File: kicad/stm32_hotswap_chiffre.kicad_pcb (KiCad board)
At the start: 2 copper layers, 227.3 x 85 mm, 108 parts, among them J1 USB_C_Receptacle_USB2.0, J101 Conn_01x03_Female, J2 OLED I2C, SW1 SW_Push, SW10 SW_Push, SW11 SW_Push, SW12 SW_Push, SW13 SW_Push, SW14 SW_Push, SW15 SW_Push, SW16 SW_Push, SW17 SW_Push, SW18 SW_Push, SW19 SW_Push, SW2 SW_Push, SW20 SW_Push, SW21 SW_Push, SW22 SW_Push, SW23 SW_Push, SW24 SW_Push, SW25 SW_Push, SW26 SW_Push, SW27 SW_Push, SW28 SW_Push, SW29 SW_Push, SW3 SW_Push, SW30 SW_Push, SW31 SW_Push, SW32 SW_Push, SW33 SW_Push, SW34 SW_Push, SW35 SW_Push, SW36 Rotary_Encoder_Switch, SW37 SKQGABE010, SW4 SW_Push, SW5 SW_Push, SW6 SW_Push, SW7 SW_Push, SW8 SW_Push, SW9 SW_Push, U1 STM32F072CBT6, U2 PRTR5V0U2X, U3 XC6206PxxxMR-Regulator_Linear

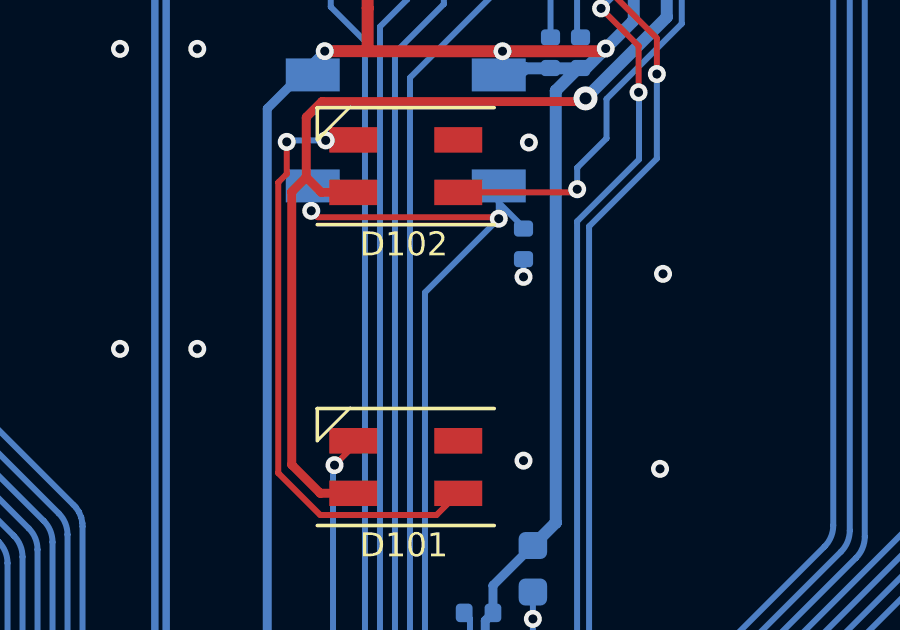
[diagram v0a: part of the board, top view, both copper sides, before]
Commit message: adding front LED bypass jumper
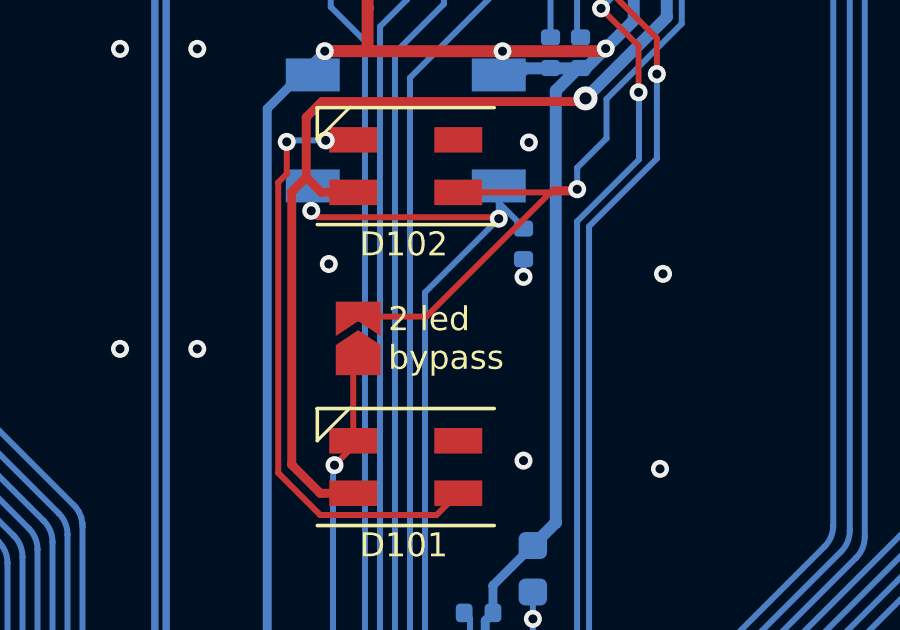
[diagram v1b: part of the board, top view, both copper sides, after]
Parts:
- added led: Jumper_2_Open, Jumper:SolderJumper-2_P1.3mm_Open_TrianglePad1.0x1.5mm, F.Cu at (145.1, 108.5)
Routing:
- net Net-(D102-DOUT): track 60.6 -> 69.7 mm
- net RGB: track 7.39 -> 10.1 mm
- net GND: vias 128 -> 129
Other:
- board text added: "2 led bypass"
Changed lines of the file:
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@@
   (title_block
     (title "Le Chiffre STM32")
-    (date "2023-07-09")
-    (rev "v0.2")
+    (date "2023-07-13")
+    (rev "v0.2.1")
     (company "sporkus")
   )
@@
     )
   )
+  (footprint "Jumper:SolderJumper-2_P1.3mm_Open_TrianglePad1.0x1.5mm" (layer "F.Cu")
+    (at 145.054472 108.55 90)
+    (descr "SMD Solder Jumper, 1x1.5mm Triangular Pads, 0.3mm gap, open")
+    (tags "solder jumper open")
+    (property "Sheetfile" "rgb.kicad_sch")
+    (property "Sheetname" "RGB leds")
+    (property "ki_description" "Jumper, 2-pole, open")
+    (property "ki_keywords" "Jumper SPST")
+    (attr exclude_from_pos_files)
+    (fp_text reference "led" (at 0.8 4.74 180) (layer "F.SilkS") hide
+        (effects (font (size 0.8 0.8) (thickness 0.15)))
+    )
+    (fp_text value "Jumper_2_Open" (at 0 1.9 90) (layer "F.Fab")
+        (effects (font (size 1 1) (thickness 0.15)))
+    )
+    (fp_line (start -1.65 -1.25) (end -1.65 1.25)
+      (stroke (width 0.05) (type solid)) (layer "F.CrtYd"))
+    (fp_line (start -1.65 -1.25) (end 1.65 -1.25)
+      (stroke (width 0.05) (type solid)) (layer "F.CrtYd"))
+    (fp_line (start 1.65 1.25) (end -1.65 1.25)
+      (stroke (width 0.05) (type solid)) (layer "F.CrtYd"))
+    (fp_line (start 1.65 1.25) (end 1.65 -1.25)
+      (stroke (width 0.05) (type solid)) (layer "F.CrtYd"))
+    (pad "1" smd custom (at -0.725 0 90) (size 0.3 0.3) (layers "F.Cu" "F.Mask")
+      (net 8 "RGB") (pinfunction "A") (pintype "passive") (zone_connect 2) (thermal_bridge_angle 45)
+      (options (clearance outline) (anchor rect))
+      (primitives
+        (gr_poly
+          (pts
+            (xy 1 0)
+            (xy 0.5 0.75)
+            (xy -0.5 0.75)
+            (xy -0.5 -0.75)
+            (xy 0.5 -0.75)
+          )
+          (width 0) (fill yes))
+      ))
+    (pad "2" smd custom (at 0.725 0 90) (size 0.3 0.3) (layers "F.Cu" "F.Mask")
+      (net 78 "Net-(D102-DOUT)") (pinfunction "B") (pintype "passive") (zone_connect 2) (thermal_bridge_angle 45)
+      (options (clearance outline) (anchor rect))
+      (primitives
+        (gr_poly
+          (pts
+            (xy 0.5 0.75)
+            (xy -0.65 0.75)
+            (xy -0.15 0)
+            (xy -0.65 -0.75)
+            (xy 0.5 -0.75)
+          )
+          (width 0) (fill yes))
+      ))
+  )
   (footprint "modified_footrprints:RotaryEncoder_EC11_no_mp" (layer "F.Cu")
     (at 146.639472 84.358057 90)
@@
     (effects (font (size 0.8 0.8) (thickness 0.15) bold) (justify mirror))
   )
+  (gr_text "2 led\nbypass" (at 146.054472 108.55) (layer "F.SilkS")
+    (effects (font (size 0.8 0.8) (thickness 0.15)) (justify left))
+  )
   (gr_text "sda" (at 150.550698 94.075) (layer "F.SilkS")
     (effects (font (size 0.8 0.8) (thickness 0.15) bold))
@@
   (via (at 256.139472 100.475) (size 0.6) (drill 0.3) (layers "F.Cu" "B.Cu") (free) (net 1))
   (via (at 146.529979 124.313523) (size 0.6) (drill 0.3) (layers "F.Cu" "B.Cu") (free) (net 1))
+  (via (at 144.074472 106.07) (size 0.6) (drill 0.3) (layers "F.Cu" "B.Cu") (free) (net 1))
   (via (at 143.589472 121.058057) (size 0.6) (drill 0.3) (layers "F.Cu" "B.Cu") (net 1))
   (via (at 149.628287 124.077799) (size 0.6) (drill 0.3) (layers "F.Cu" "B.Cu") (net 1))
@@
   (segment (start 145.689473 88.858056) (end 147.797528 86.75) (width 0.2) (layer "B.Cu") (net 7))
   (segment (start 144.814327 112.225145) (end 144.814327 112.038203) (width 0.2) (layer "F.Cu") (net 8))
+  (segment (start 144.889472 111.963058) (end 144.889472 109.44) (width 0.2) (layer "F.Cu") (net 8))
+  (segment (start 144.889472 109.44) (end 145.054472 109.275) (width 0.2) (layer "F.Cu") (net 8))
   (segment (start 144.264472 112.775) (end 144.814327 112.225145) (width 0.2) (layer "F.Cu") (net 8))
   (via (at 144.264472 112.775) (size 0.6) (drill 0.3) (layers "F.Cu" "B.Cu") (net 8))
@@
   (segment (start 143.971268 101.95) (end 142.722268 101.95) (width 0.2) (layer "B.Cu") (net 77))
   (segment (start 152.248787 103.683056) (end 148.389472 103.683056) (width 0.2) (layer "F.Cu") (net 78))
+  (segment (start 145.054472 107.825) (end 147.323529 107.825) (width 0.2) (layer "F.Cu") (net 78))
   (segment (start 152.353786 103.578057) (end 152.248787 103.683056) (width 0.2) (layer "F.Cu") (net 78))
+  (segment (start 151.570472 103.578057) (end 152.353786 103.578057) (width 0.2) (layer "F.Cu") (net 78))
+  (segment (start 147.323529 107.825) (end 151.570472 103.578057) (width 0.2) (layer "F.Cu") (net 78))
   (via (at 152.353786 103.578057) (size 0.6) (drill 0.3) (layers "F.Cu" "B.Cu") (net 78))
   (segment (start 152.353786 103.578057) (end 152.353785 102.860685) (width 0.2) (layer "B.Cu") (net 78))

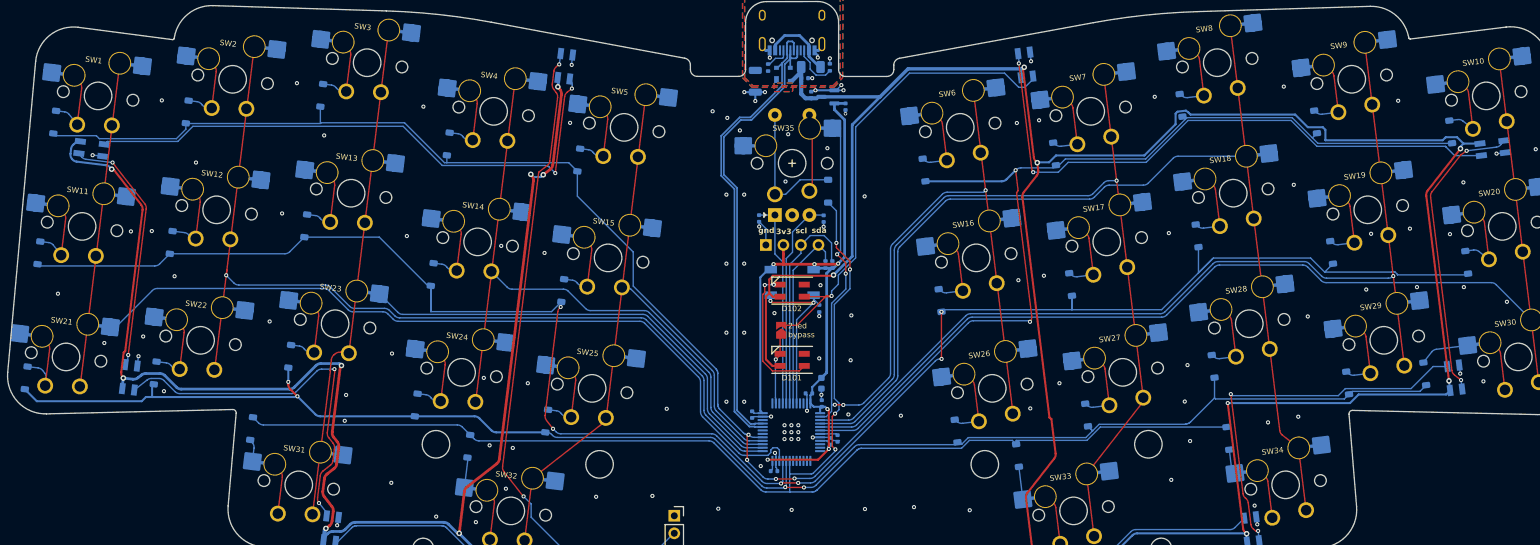
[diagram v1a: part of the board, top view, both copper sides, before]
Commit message: change center switch footprint
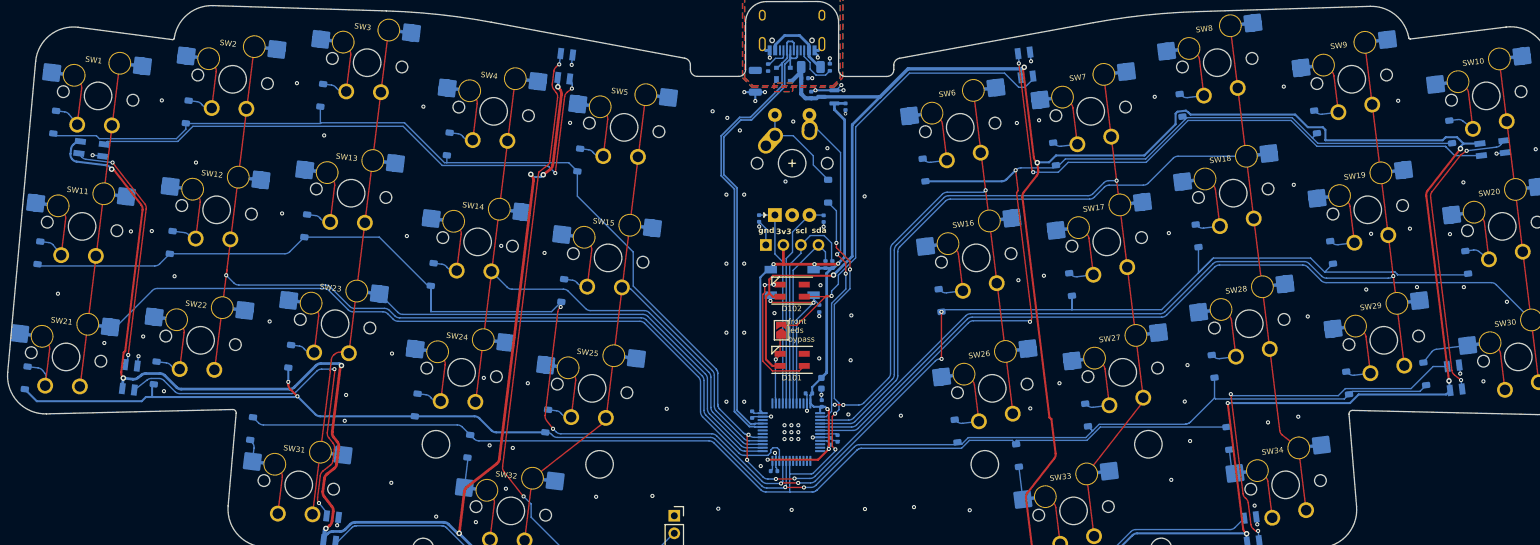
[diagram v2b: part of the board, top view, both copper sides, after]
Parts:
- removed led: Jumper_2_Open, Jumper:SolderJumper-2_P1.3mm_Open_TrianglePad1.0x1.5mm
- added JP2: Jumper_2_Open, Jumper:SolderJumper-2_P1.3mm_Open_TrianglePad1.0x1.5mm, F.Cu at (145.1, 108.5)
- SW35: footprint MX_hotswap_alps:MX-Hotswap-Alps-1U -> MX_Alps_Hybrid:MX-Alps-Hybrid-1U
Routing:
- net col5: track 148.3 -> 140.6 mm
- net Net-(D35-K): track 20.1 -> 14.1 mm
- net Net-(D13-K): track 11.2 -> 8.99 mm
- net Net-(D14-K): track 11.2 -> 8.99 mm
- net Net-(D23-K): track 11.2 -> 8.99 mm
- net Net-(D4-K): track 11.2 -> 8.99 mm
- net Net-(D25-K): track 11.2 -> 8.99 mm
- net Net-(D5-K): track 11.2 -> 8.99 mm
- net Net-(D15-K): track 11.2 -> 8.99 mm
- net Net-(D24-K): track 11.2 -> 8.99 mm
- net Net-(D2-K): track 11.2 -> 8.99 mm
- net Net-(D3-K): track 11.2 -> 8.99 mm
- net col2: track 139.9 -> 138.3 mm
- net Net-(D28-K): track 11.2 -> 9.77 mm
- net Net-(D11-K): track 11.4 -> 9.99 mm
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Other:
- board text added: "front leds bypass"
- board text removed: "2 led bypass"
